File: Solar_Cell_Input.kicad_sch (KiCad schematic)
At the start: 36 parts, among them Q201 NMOS, Q202 NMOS, Q203 NMOS, Q204 NMOS, U201 BQ24650

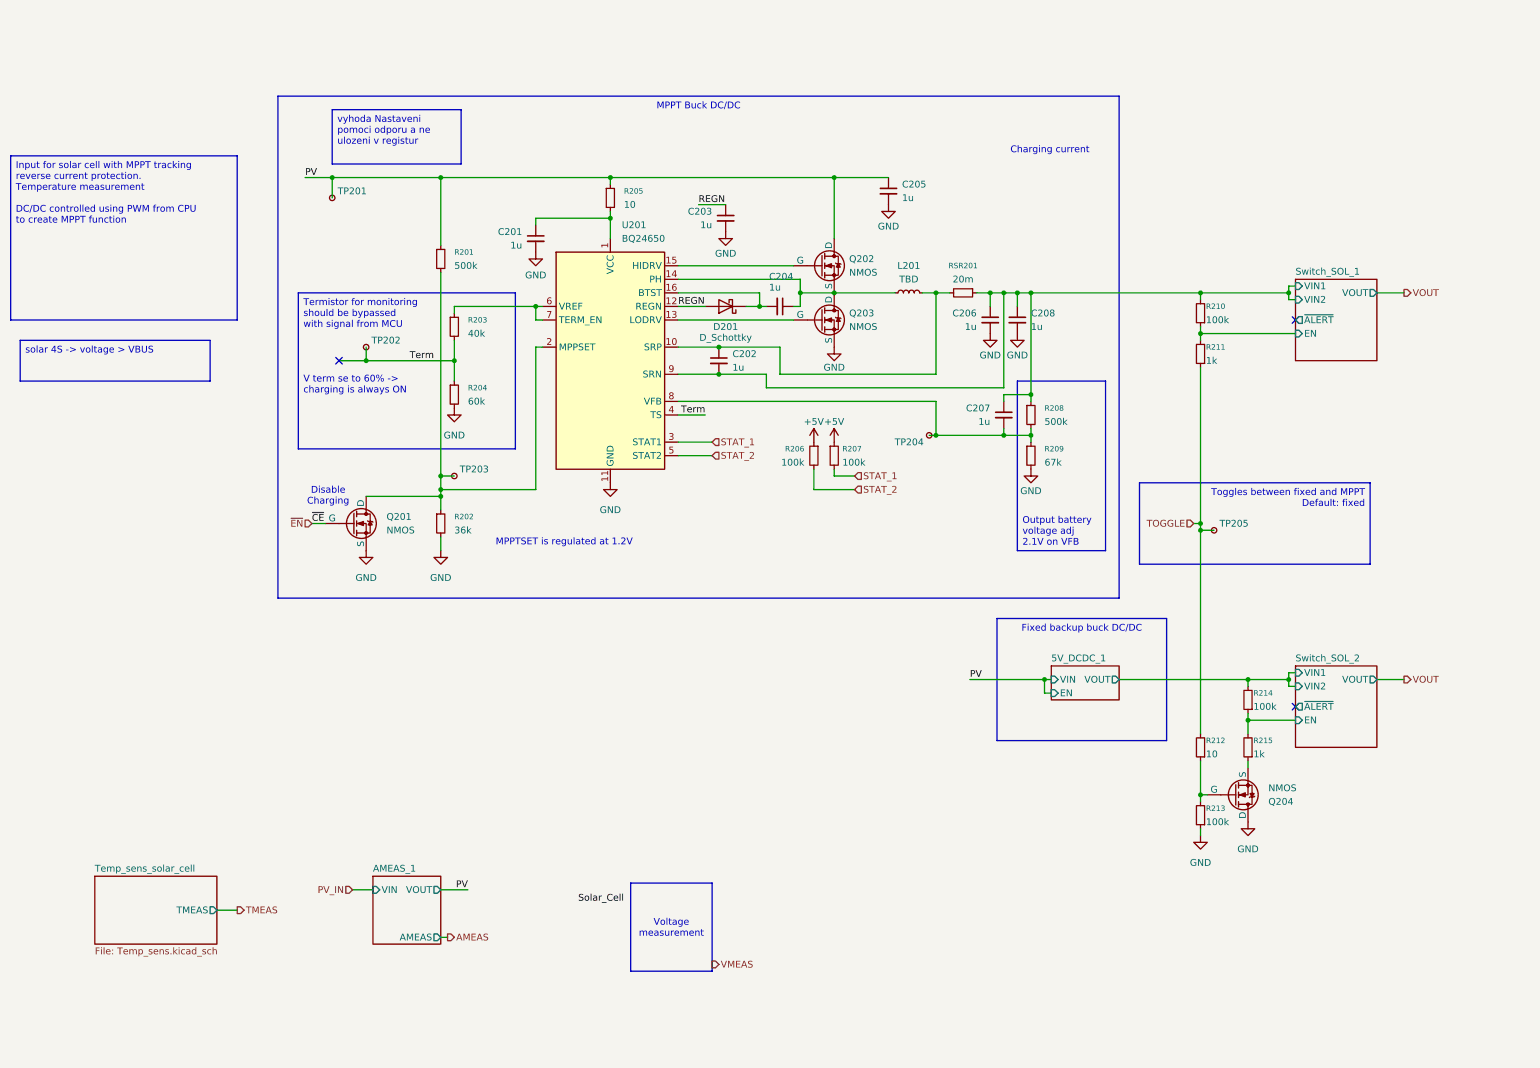
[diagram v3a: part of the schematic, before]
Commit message: reduced number of DCDC converter for PV panels; updated test pcb
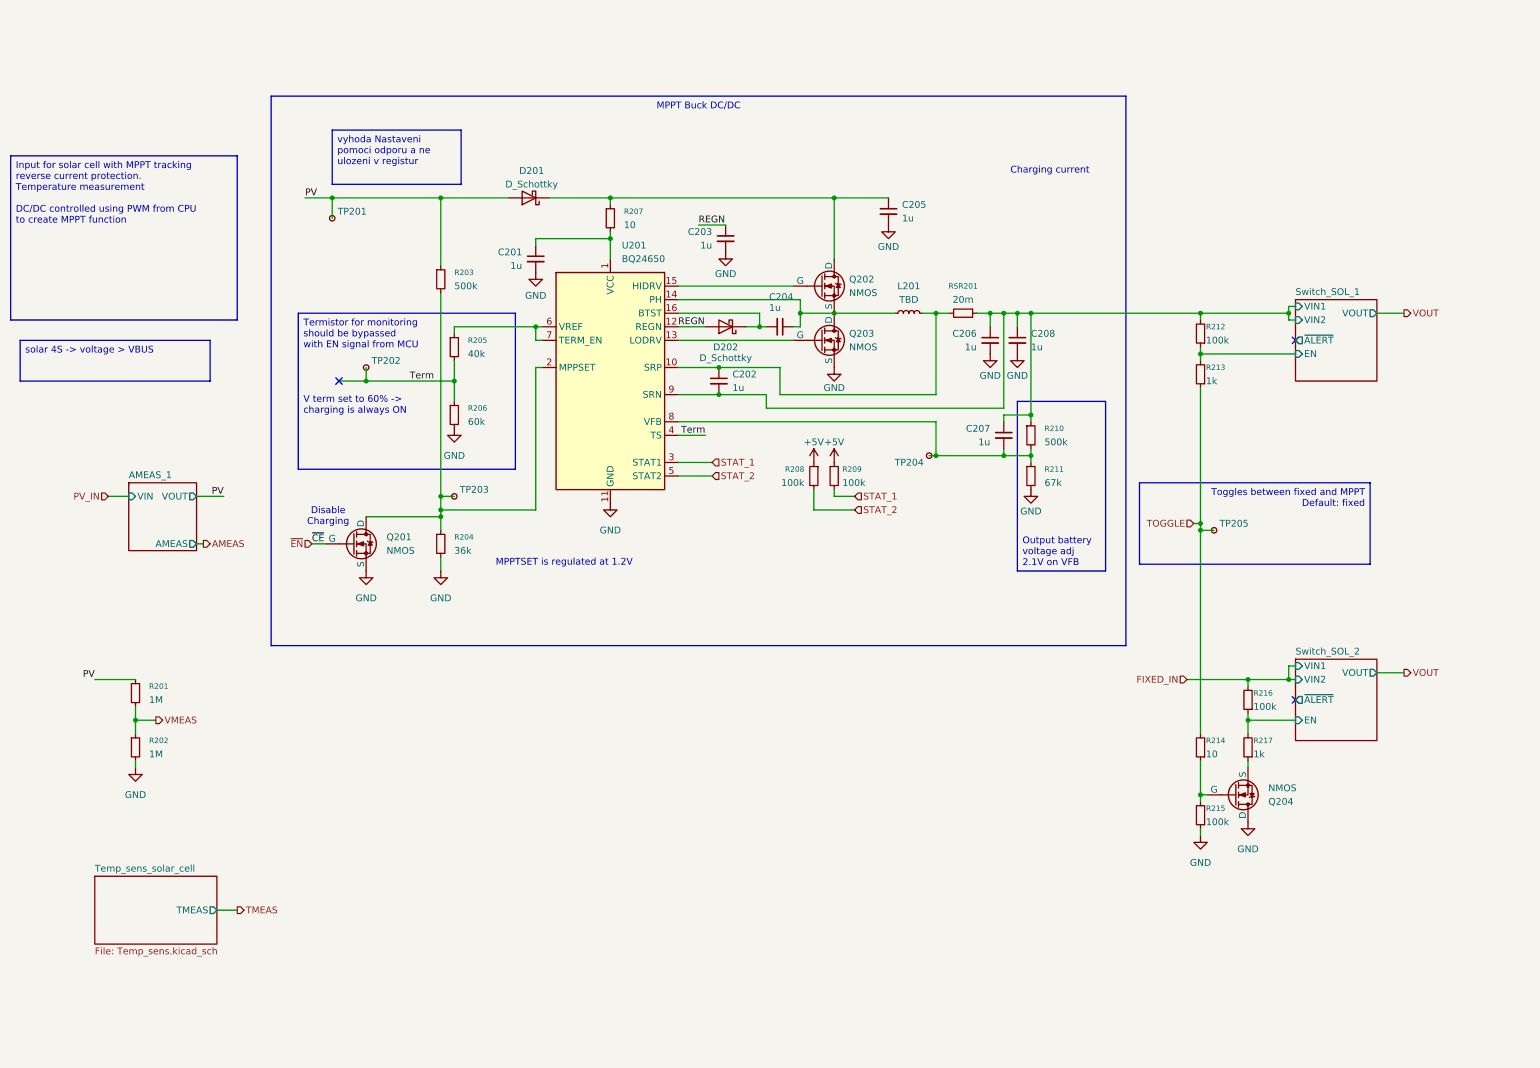
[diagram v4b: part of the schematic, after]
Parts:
- added D201: D_Schottky, Diode_SMD:D_0805_2012Metric, symbol Device:D_Schottky
- added R201, R202: 1M, Resistor_SMD:R_0603_1608Metric_Pad0.98x0.95mm_HandSolder, symbol Device:R_Small
- L201: footprint Inductor_SMD:L_Taiyo-Yuden_NR-10050_9.8x10.0mm_HandSoldering -> Inductor_SMD:L_6.3x6.3_H3
- Q202, Q203: footprint Package_TO_SOT_SMD:SOT-23-3 -> Outlines:NVTFS5116PLTWG
- renumbered D201 to D202, R201 to R203, R202 to R204, R203 to R205, R204 to R206, R205 to R207, R206 to R208, R207 to R209, R208 to R210, R209 to R211, R210 to R212, R211 to R213, R212 to R214, R213 to R215, R214 to R216, R215 to R217
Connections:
- net GND: now also R202.2
- net PV: now also D201.2 (A), R201.1; no longer C205.1, Q202.1 (D), R207.1
- net VMEAS: now also R201.2, R202.1
- net 5V_DCDC_1/VOUT renamed FIXED_IN
- new net: C205.1, D201.1 (K), Q202.1 (D), R207.1
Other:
- removed sheet 5V_DCDC_1
- moved on the sheet: C201, C202, C203, C204, C205, C206, C207, C208, D202, L201, Q201, Q202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

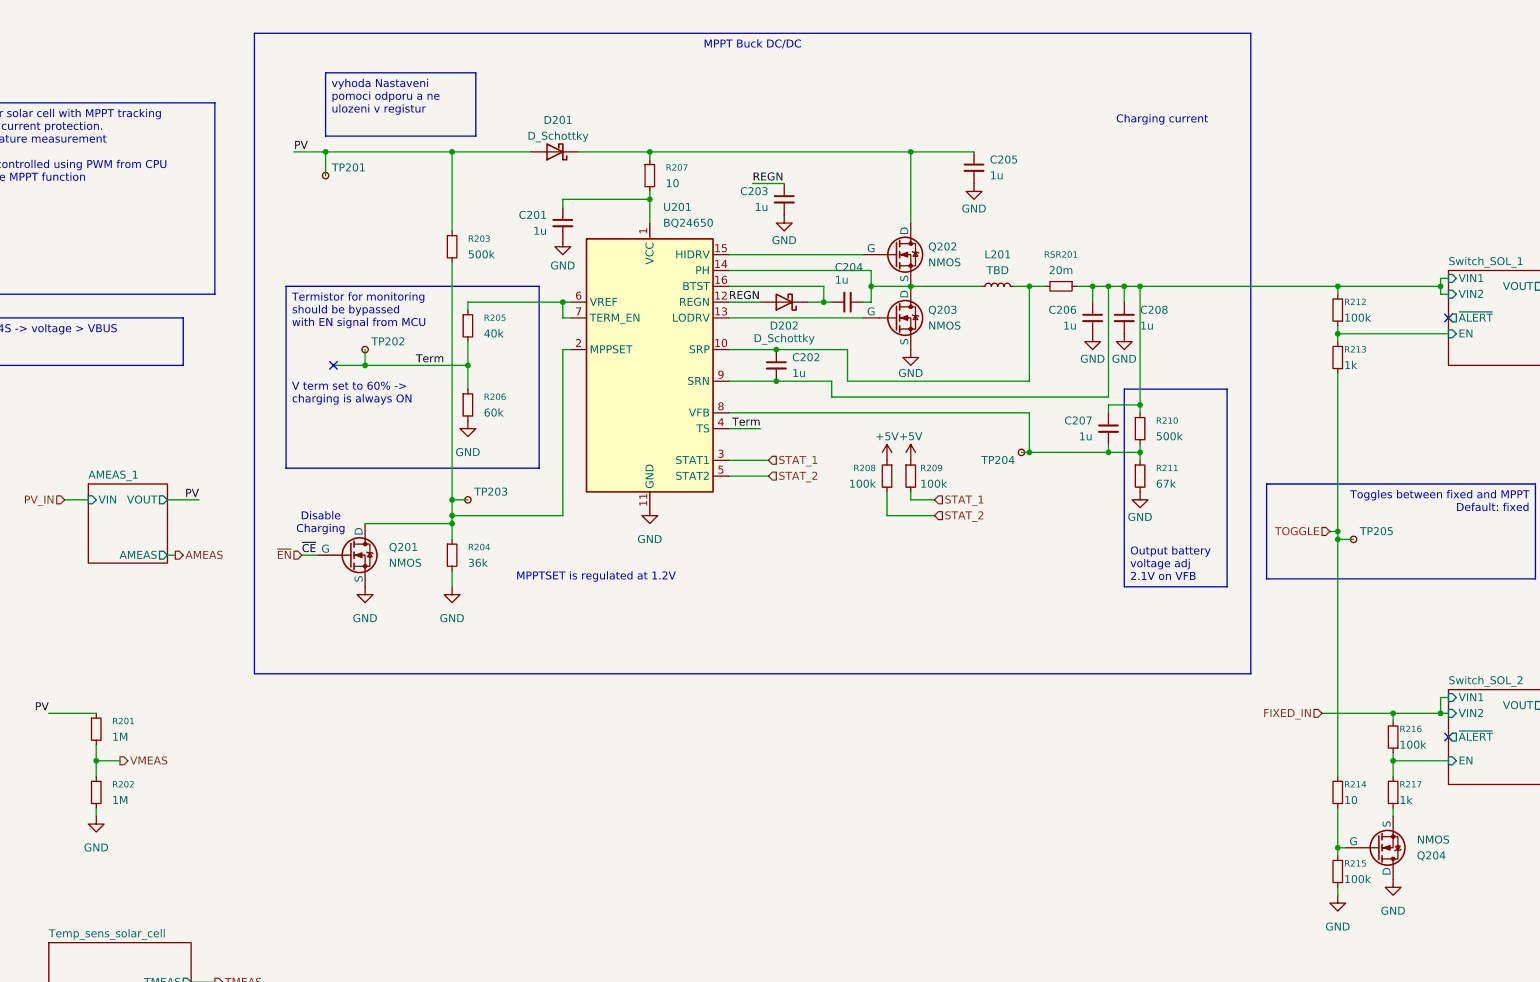
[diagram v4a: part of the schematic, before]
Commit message: added missing heater connectors
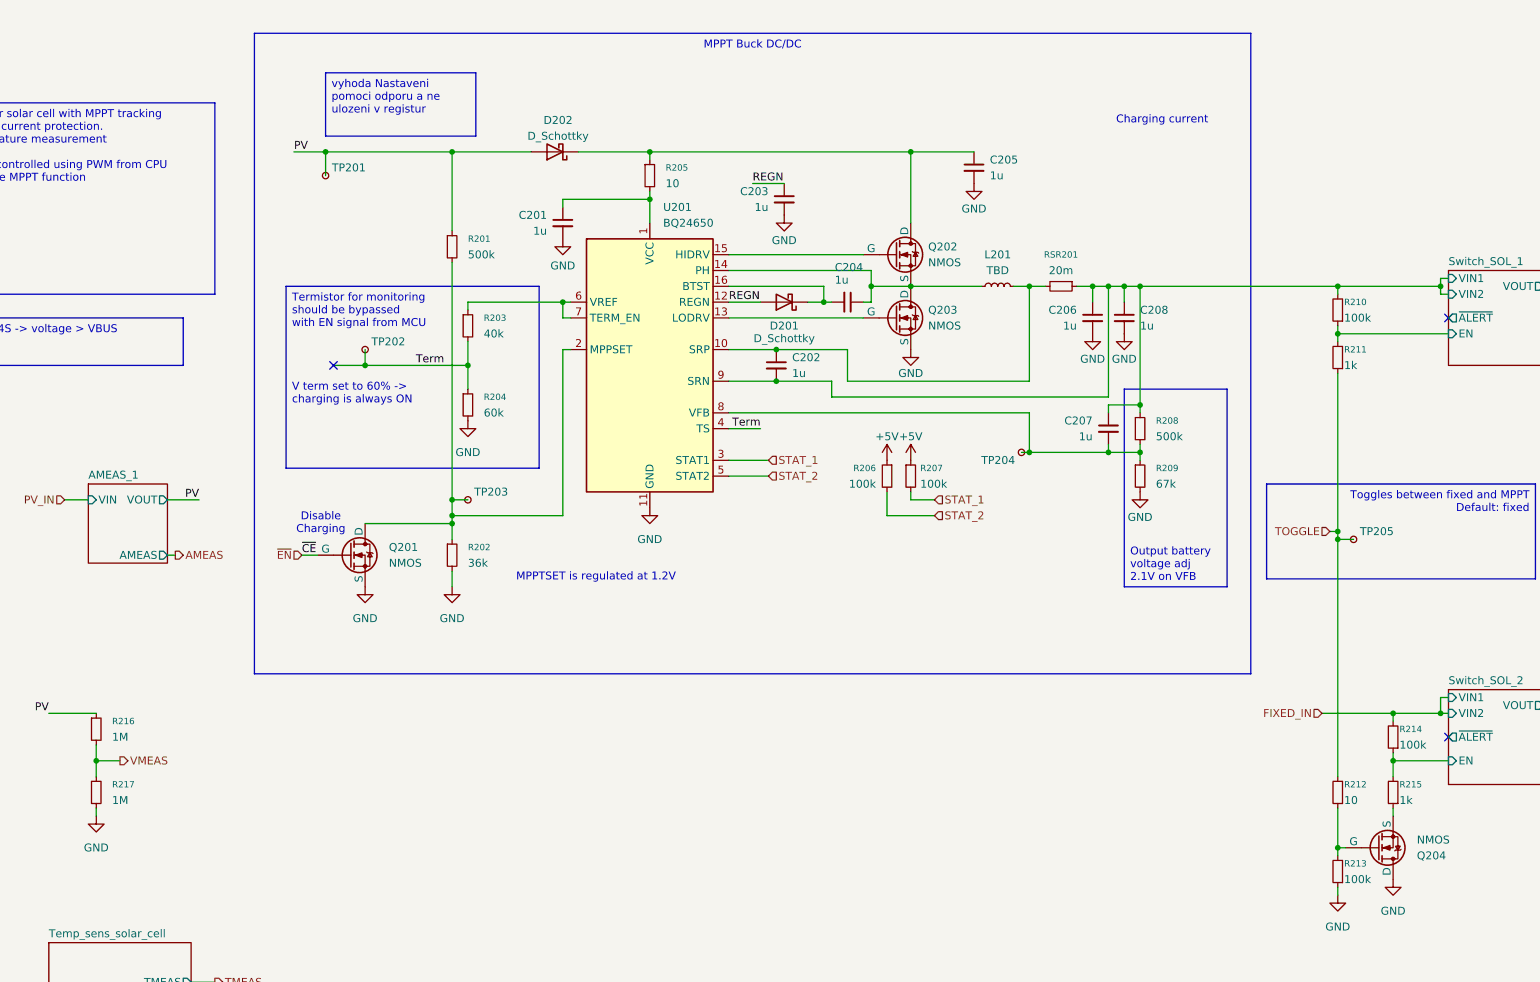
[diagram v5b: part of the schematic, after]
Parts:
- RSR201: footprint Resistor_SMD:R_0603_1608Metric_Pad0.98x0.95mm_HandSolder -> Resistor_SMD:R_1210_3225Metric_Pad1.30x2.65mm_HandSolder
- renumbered D202 to D201, D201 to D202, R203 to R201, R204 to R202, R205 to R203, R206 to R204, R207 to R205, R208 to R206, R209 to R207, R210 to R208, R211 to R209, R212 to R210, R213 to R211, R214 to R212, R215 to R213, R216 to R214, R217 to R215, R201 to R216, R202 to R217
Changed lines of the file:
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@@
 		(dnp no)
 		(fields_autoplaced yes)
-		(property "Reference" "R202"
+		(property "Reference" "R217"
 			(at 41.91 140.9699 0)
 			(effects
@@
 			)
 		)
-		(property "Footprint" "Resistor_SMD:R_0603_1608Metric_Pad0.98x0.95mm_HandSolder"
+		(property "Footprint" "Resistor_SMD:R_1210_3225Metric_Pad1.30x2.65mm_HandSolder"
 			(at 194.31 60.96 0)
 			(effects
@@
 		(dnp no)
 		(fields_autoplaced yes)
-		(property "Reference" "R207"
+		(property "Reference" "R205"
 			(at 130.81 41.9099 0)
 			(effects
@@
 		(on_board yes)
 		(dnp no)
-		(property "Reference" "R209"
+		(property "Reference" "R207"
 			(at 171.704 90.17 0)
 			(effects
@@
 		(on_board yes)
 		(dnp no)
-		(property "Reference" "#PWR0213"
+		(property "Reference" "#PWR0212"
 			(at 204.47 74.93 0)
 			(effects
@@
 		(on_board yes)
 		(dnp no)
-		(property "Reference" "#PWR0208"
+		(property "Reference" "#PWR0207"
 			(at 166.37 92.71 0)
 			(effects
@@
 		(on_board yes)
 		(dnp no)
-		(property "Reference" "#PWR0211"
+		(property "Reference" "#PWR0210"
 			(at 180.34 50.8 0)
 			(effects
@@
 		(dnp no)
 		(fields_autoplaced yes)
-		(property "Reference" "R206"
+		(property "Reference" "R204"
 			(at 101.6 78.7399 0)
 			(effects
@@
 		(dnp no)
 		(fields_autoplaced yes)
-		(property "Reference" "R205"
+		(property "Reference" "R203"
 			(at 101.6 66.0399 0)
 			(effects
@@
 		(on_board yes)
 		(dnp no)
-		(property "Reference" "R213"
+		(property "Reference" "R211"
 			(at 239.776 71.12 0)
 			(effects
@@
 		(dnp no)
 		(fields_autoplaced yes)
-		(property "Reference" "#PWR0206"
+		(property "Reference" "#PWR0205"
 			(at 128.27 102.87 0)
 			(effects
@@
 		(on_board yes)
 		(dnp no)
-		(property "Reference" "#PWR0205"
+		(property "Reference" "#PWR0204"
 			(at 114.3 59.69 0)
 			(effects
@@
 		(dnp no)
 		(fields_autoplaced yes)
-		(property "Reference" "#PWR0203"
+		(property "Reference" "#PWR0202"
 			(at 96.52 115.57 0)
 			(effects
@@
 		(on_board yes)
 		(dnp no)
-		(property "Reference" "R212"
+		(property "Reference" "R210"
 			(at 239.776 63.5 0)
 			(effects
@@
 		(dnp no)
 		(fields_autoplaced yes)
-		(property "Reference" "R203"
+		(property "Reference" "R201"
 			(at 99.06 53.3399 0)
 			(effects
@@
 		(dnp no)
 		(fields_autoplaced yes)
-		(property "Reference" "#PWR0215"
+		(property "Reference" "#PWR0214"
 			(at 238.76 165.1 0)
 			(effects
@@
 		(on_board yes)
 		(dnp no)
-		(property "Reference" "#PWR0212"
+		(property "Reference" "#PWR0211"
 			(at 199.39 74.93 0)
 			(effects
@@
 		(on_board yes)
 		(dnp no)
-		(property "Reference" "R217"
+		(property "Reference" "R215"
 			(at 248.666 140.97 0)
 			(effects
@@
 		(dnp no)
 		(fields_autoplaced yes)
-		(property "Reference" "#PWR0201"
+		(property "Reference" "#PWR0216"
 			(at 39.37 152.4 0)
 			(effects
@@
 		(dnp no)
 		(fields_autoplaced yes)
-		(property "Reference" "R210"
+		(property "Reference" "R208"
 			(at 209.55 82.5499 0)
 			(effects
@@
 		(on_board yes)
 		(dnp no)
-		(property "Reference" "#PWR0209"
+		(property "Reference" "#PWR0208"
 			(at 170.18 77.47 0)
 			(effects
@@
 		(dnp no)
 		(fields_autoplaced yes)
-		(property "Reference" "R201"
+		(property "Reference" "R216"
 			(at 41.91 130.8099 0)
 			(effects
@@
 		(on_board yes)
 		(dnp no)
-		(property "Reference" "#PWR0214"
+		(property "Reference" "#PWR0213"
 			(at 207.01 100.33 0)
 			(effects
@@
 		(dnp no)
 		(fields_autoplaced yes)
-		(property "Reference" "#PWR0202"
+		(property "Reference" "#PWR0201"
 			(at 82.55 115.57 0)
 			(effects
@@
 		(on_board yes)
 		(dnp no)
-		(property "Reference" "#PWR0210"
+		(property "Reference" "#PWR0209"
 			(at 170.18 92.71 0)
 			(effects
@@
 		(on_board yes)
 		(dnp no)
-		(property "Reference" "R208"
+		(property "Reference" "R206"
 			(at 164.592 90.17 0)
 			(effects
@@
 		(dnp no)
 		(fields_autoplaced yes)
-		(property "Reference" "R204"
+		(property "Reference" "R202"
 			(at 99.06 102.8699 0)
 			(effects
@@
 		(on_board yes)
 		(dnp no)
-		(property "Reference" "#PWR0207"
+		(property "Reference" "#PWR0206"
 			(at 149.86 55.88 0)
 			(effects
@@
 		(on_board yes)
 		(dnp no)
-		(property "Reference" "R216"
+		(property "Reference" "R214"
 			(at 248.666 132.08 0)
 			(effects
@@
 		(dnp no)
 		(fields_autoplaced yes)
-		(property "Reference" "#PWR0216"
+		(property "Reference" "#PWR0215"
 			(at 247.65 162.56 0)
 			(effects
@@
 		(on_board yes)
 		(dnp no)
-		(property "Reference" "R215"
+		(property "Reference" "R213"
 			(at 239.776 153.67 0)
 			(effects
@@
 		(dnp no)
 		(fields_autoplaced yes)
-		(property "Reference" "#PWR0204"
+		(property "Reference" "#PWR0203"
 			(at 99.06 88.9 0)
 			(effects
@@
 		(on_board yes)
 		(dnp no)
-		(property "Reference" "D202"
+		(property "Reference" "D201"
 			(at 149.86 67.31 0)
 			(effects
@@
 		(on_board yes)
 		(dnp no)
-		(property "Reference" "R214"
+		(property "Reference" "R212"
 			(at 239.776 140.97 0)
 			(effects
@@
 		(dnp no)
 		(fields_autoplaced yes)
-		(property "Reference" "R211"
+		(property "Reference" "R209"
 			(at 209.55 90.1699 0)
 			(effects
@@
 		(on_board yes)
 		(dnp no)
-		(property "Reference" "D201"
+		(property "Reference" "D202"
 			(at 113.538 34.29 0)
 			(effects

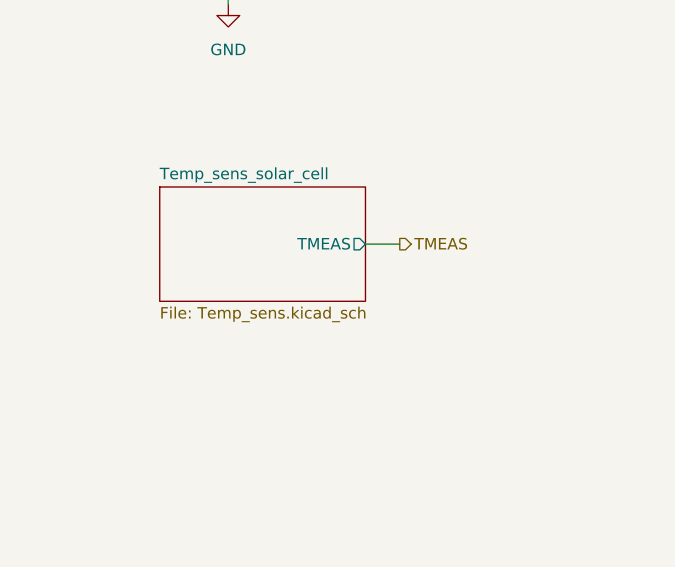
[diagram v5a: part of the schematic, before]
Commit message: replaced individual CC sourses for SOL with a single one
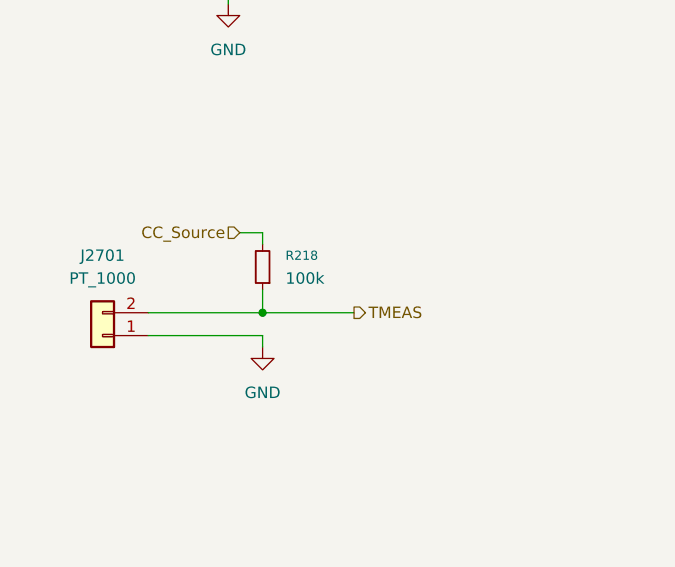
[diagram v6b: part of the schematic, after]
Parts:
- added J2701: PT_1000, Connector_PinSocket_2.54mm:PinSocket_1x02_P2.54mm_Vertical, symbol Connector_Generic:Conn_01x02
- added R218: 100k, Resistor_SMD:R_0603_1608Metric_Pad0.98x0.95mm_HandSolder, symbol Device:R_Small
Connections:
- net GND: now also J2701.1 (Pin_1)
- net TMEAS: now also J2701.2 (Pin_2), R218.1
- new net CC_Source: R218.2
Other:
- removed sheet Temp_sens_solar_cell
